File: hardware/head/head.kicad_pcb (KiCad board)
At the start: 2 copper layers, 80 x 55 mm, 59 parts, among them J1 Head bundle, J10 CM4 socket 101-200, J11 Ext amp, J12 Ext 5V, J13 SPI pads, J2 ToF, J3 I2C breakout, J4 Eye LED, J5 Speaker, J6 Fan, J7 Microphone, J8 Camera, J9 CM4 socket 1-100, Q1 AO3400A, U2 LMR51635YDDCR, U3 AMS1117-3.3, U4 MAX98357AETE+T, U5 BMI088

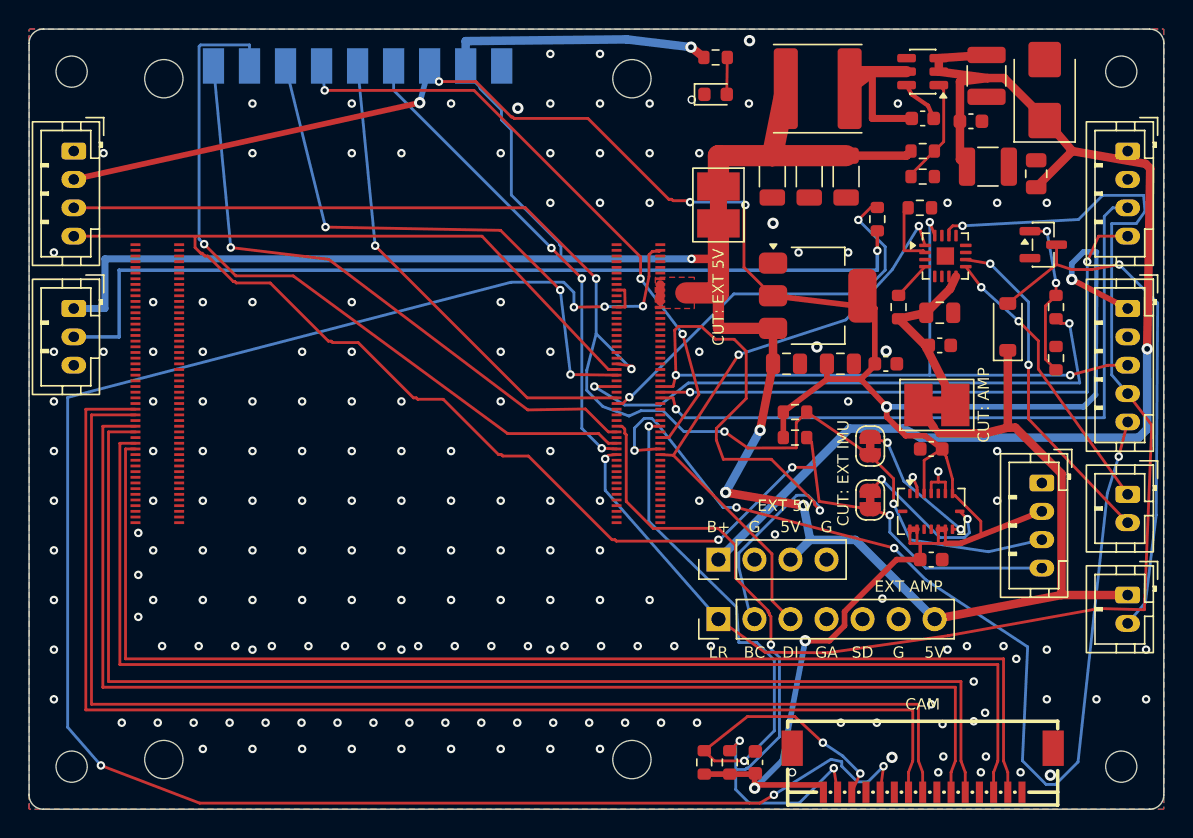
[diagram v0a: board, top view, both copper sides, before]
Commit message: Head carrier PCB rev B: pre-order review changes, USB download pads
- Buck input loop: C4 straight across U2's VIN and GND pins with ground
  vias beside them; boot cap and feedback divider at their pins.
- Input chain J1, TVS, C17 (47 uF 50 V electrolytic, C970679), then the
  ceramics; C3 dropped; fan parts moved down.
- 330R series resistors (R13, R14) in the link UART; J1 pins 3 and 4
  are now LINK_RX and LINK_TX.
- Bottom test pads: RST and BOOT (CM4 pins 92, 93), and USB D+, D-, G
  for the RK3576 download port (pins 105, 103) to flash in place.
  Pins checked against Radxa's CM4 schematic v1.20, sheets 8, 21, 22.
- J13 moved 2.5 mm clear of the module's M2.5 holes; J8 ends marked
  1 GND and 15 3V3.
- Top-layer keep-outs across the cut lines of JP1, JP3, JP4 and JP5
  (no tracks, vias or pour); crossing tracks rerouted.
- Tools: tidy and route_one_net treat locked copper of other nets as
  obstacles; tidy takes a board name, keeps socket ground tracks, never
  straightens through a pad, undangle runs one pass per process;
  route_one_net takes PCB, W, SRC and DST from the environment.
- DRC 0 violations with schematic parity; J9 pad 23 (ground, boxed in)
  unconnected, grounded inside the module. JLC package, PDFs and renders
  regenerated; design note sections 4 and 9.4.
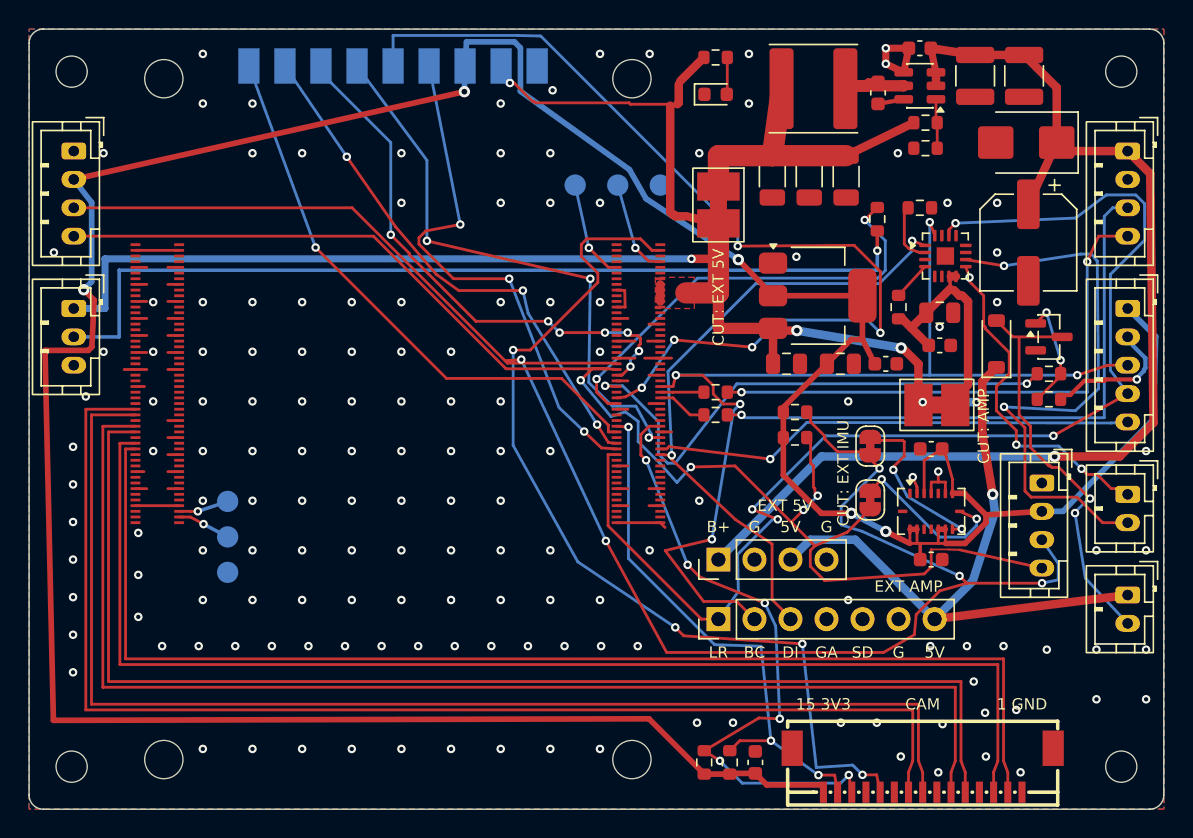
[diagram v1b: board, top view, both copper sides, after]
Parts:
- removed C3: 2.2u 50V, Capacitor_SMD:C_0805_2012Metric
- added C17: 47u 50V, Capacitor_SMD:CP_Elec_6.3x7.7, F.Cu at (170.4, 65.0)
- added R13: 330R, Resistor_SMD:R_0603_1608Metric, F.Cu at (148.4, 77.2)
- added R14: 330R, Resistor_SMD:R_0603_1608Metric, F.Cu at (148.4, 75.6)
- added TP1: CM4_RESET, TestPoint:TestPoint_Pad_D1.5mm, B.Cu at (138.5, 61.0)
- added TP2: CM4_MASKROM, TestPoint:TestPoint_Pad_D1.5mm, B.Cu at (141.5, 61.0)
- added TP3: GND, TestPoint:TestPoint_Pad_D1.5mm, B.Cu at (144.5, 61.0)
- added TP4: USB_DN, TestPoint:TestPoint_Pad_D1.5mm, B.Cu at (114.0, 85.8)
- added TP5: USB_DP, TestPoint:TestPoint_Pad_D1.5mm, B.Cu at (114.0, 83.3)
- added TP6: GND, TestPoint:TestPoint_Pad_D1.5mm, B.Cu at (114.0, 88.3)
- moved C2 6.89 mm to (170.2, 53.3), turned to -90 degrees
- moved Q1 6.51 mm to (171.9, 71.7)
- moved C4 6.28 mm to (162.8, 51.4), turned to 180 degrees
- moved R5 4.73 mm to (171.9, 74.3), turned to 0 degrees
- moved D1 3.92 mm to (170.3, 58.0), turned to 180 degrees
- moved C5 3.63 mm to (159.8, 54.5), turned to 90 degrees
- moved R6 2.94 mm to (171.9, 76.1), turned to 0 degrees
- moved J13 2.50 mm to (135.8, 52.6)
- moved R1 2.01 mm to (163.2, 56.6)
- moved R2 2.01 mm to (163.2, 58.4), turned to 180 degrees
- moved D2 1.44 mm to (168.2, 72.2)
- moved U2 1.02 mm to (162.8, 54.0)
- moved C1 0.80 mm to (166.7, 53.3)
- moved L1 0.30 mm to (155.3, 54.2)
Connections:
- J1 pad 3: /UART7_RX -> /LINK_RX
- J1 pad 4: /UART7_TX -> /LINK_TX
- J10 pad 103: unconnected-(J10-USB2_N-Pad103) -> /USB_DN
- J10 pad 105: unconnected-(J10-USB2_P-Pad105) -> /USB_DP
- J9 pad 92: unconnected-(J9-RUN_PG-Pad92) -> /CM4_RESET
- J9 pad 93: unconnected-(J9-nRPIBOOT-Pad93) -> /CM4_MASKROM
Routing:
- net /CAM_GPIO: track 134.0 -> 65.4 mm, vias 6 -> 4
- net +3V3: track 180.7 -> 241.1 mm, vias 8 -> 5
- net GND: track 4.56 -> 61.7 mm, vias 181 -> 153
- net /UART7_RX: track 48.3 -> 3.57 mm, vias 1 -> 0
- net /LINK_RX: track 0.00 -> 42.8 mm, vias 0 -> 1
- net /SAI2_SDI: track 74.7 -> 34.1 mm, vias 4 -> 1
- net /UART7_TX: track 43.3 -> 3.07 mm, vias 2 -> 0
- net /LINK_TX: track 0.00 -> 38.6 mm, vias 0 -> 2
- net /SPI2_MISO: track 34.2 -> 70.0 mm, vias 1 -> 5
- net /I2C8_SDA: track 92.8 -> 121.2 mm, vias 4 -> 5
- net /I2C8_SCL: track 120.1 -> 98.7 mm, vias 3 -> 4
- net /SPK_N: track 23.9 -> 40.6 mm
- net /SPI_INT: track 53.1 -> 37.6 mm, vias 1 -> 3
- net +5V: track 170.9 -> 158.7 mm, vias 5 -> 7
- net /SAI2_SCLK: track 84.3 -> 73.0 mm, vias 4 -> 5
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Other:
- board text added: "1 GND"
- board text added: "15 3V3"
- board text added: "BOOT"
- board text added: "D+"
- board text added: "D-"
- board text added: "RST"
- board text added: "USB"
- board text added: "rev B 2026"
- board text removed: "rev A 2026"

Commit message: Head carrier PCB: PWM pad for a possible mouth servo
- TP7, a bottom pad beside J9 on CM4 pin 37 (GPIO7, RK3576 GPIO1_C0,
  PWM0_CH0_M1), in case the mouth J288 is swapped for a hobby servo. The
  servo would run from its own buck module fed from J12's B+ and G, not
  the head's 5 V buck. PWM0 is separate from the fan's PWM1.
- Pin 48 (PWM1_CH0_M2) was tried first; on J9's inner row it is boxed in.
- Design note: J13 already gives spare GPIOs with 3V3 and GND (pads 8, 9
  and the SPI2 lines); a separate breakout under the module was tried and
  dropped (only a 130 mm, 11-via route).
- DRC 0 violations with schematic parity (J9 pad 23 as before); JLC
  package, PDFs and bottom render regenerated.
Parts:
- added TP7: SERVO_PWM, TestPoint:TestPoint_Pad_D1.5mm, B.Cu at (146.6, 77.0)
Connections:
- J9 pad 37: unconnected-(J9-GPIO7-Pad37) -> /SERVO_PWM
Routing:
- net /SERVO_PWM: track 0.00 -> 1.22 mm, vias 0 -> 1
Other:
- board text added: "PWM"
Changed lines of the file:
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@@
 			(size 0.2 0.7)
 			(layers "F.Cu" "F.Mask" "F.Paste")
-			(net "unconnected-(J9-GPIO7-Pad37)")
+			(net "/SERVO_PWM")
 		)
 		(pad "38" smd rect
@@
 		(locked yes)
 		(layer "B.Cu")
+		(at 146.55 77 180)
+		(descr "SMD pad as test Point, diameter 1.5mm")
+		(tags "test point SMD pad")
+		(property "Reference" "TP7"
+			(at 0 1.648 0)
+			(layer "B.Fab")
+			(effects
+				(font
+					(size 1 1)
+					(thickness 0.15)
+				)
+				(justify mirror)
+			)
+		)
+		(property "Value" "SERVO_PWM"
+			(at 0 -1.75 0)
+			(layer "B.Fab")
+			(hide yes)
+			(effects
+				(font
+					(size 1 1)
+					(thickness 0.15)
+				)
+				(justify mirror)
+			)
+		)
+		(property "Datasheet" ""
+			(at 0 0 0)
+			(unlocked yes)
+			(layer "B.Fab")
+			(hide yes)
+			(effects
+				(font
+					(size 1.27 1.27)
+					(thickness 0.15)
+				)
+				(justify mirror)
+			)
+		)
+		(property "Description" ""
+			(at 0 0 0)
+			(unlocked yes)
+			(layer "B.Fab")
+			(hide yes)
+			(effects
+				(font
+					(size 1.27 1.27)
+					(thickness 0.15)
+				)
+				(justify mirror)
+			)
+		)
+		(sheetname "Root")
+		(sheetfile "head.kicad_sch")
+		(attr exclude_from_pos_files exclude_from_bom)
+		(duplicate_pad_numbers_are_jumpers no)
+		(fp_circle
+			(center 0 0)
+			(end 0 -0.95)
+			(stroke
+				(width 0.12)
+				(type solid)
+			)
+			(fill no)
+			(layer "B.SilkS")
+		)
+		(fp_circle
+			(center 0 0)
+			(end 1.25 0)
+			(stroke
+				(width 0.05)
+				(type solid)
+			)
+			(fill no)
+			(layer "B.CrtYd")
+		)
+		(fp_text user "${REFERENCE}"
+			(at 0 1.65 0)
+			(layer "B.Fab")
+			(effects
+				(font
+					(size 1 1)
+					(thickness 0.15)
+				)
+				(justify mirror)
+			)
+		)
+		(pad "1" smd circle
+			(at 0 0 180)
+			(size 1.5 1.5)
+			(layers "B.Cu" "B.Mask")
+			(net "/SERVO_PWM")
+		)
+		(embedded_fonts no)
+	)
+	(footprint "TestPoint:TestPoint_Pad_D1.5mm"
+		(locked yes)
+		(layer "B.Cu")
 		(at 114 85.8 180)
 		(descr "SMD pad as test Point, diameter 1.5mm")
@@
 		)
 	)
+	(gr_text "PWM"
+		(at 148.95 77 0)
+		(layer "B.SilkS")
+		(effects
+			(font
+				(size 0.8 0.8)
+				(thickness 0.15)
+			)
+			(justify mirror)
+		)
+	)
 	(gr_text "1"
 		(at 169.3 80.1 0)
@@
 	)
 	(segment
+		(start 145.6 77.6)
+		(end 145.9 77.3)
+		(width 0.2)
+		(locked yes)
+		(layer "F.Cu")
+		(net "/SERVO_PWM")
+	)
+	(segment
+		(start 144.8 77.6)
+		(end 145.6 77.6)
+		(width 0.2)
+		(locked yes)
+		(layer "F.Cu")
+		(net "/SERVO_PWM")
+	)
+	(via
+		(at 145.9 77.3)
+		(size 0.6)
+		(drill 0.3)
+		(layers "F.Cu" "B.Cu")
+		(locked yes)
+		(net "/SERVO_PWM")
+	)
+	(segment

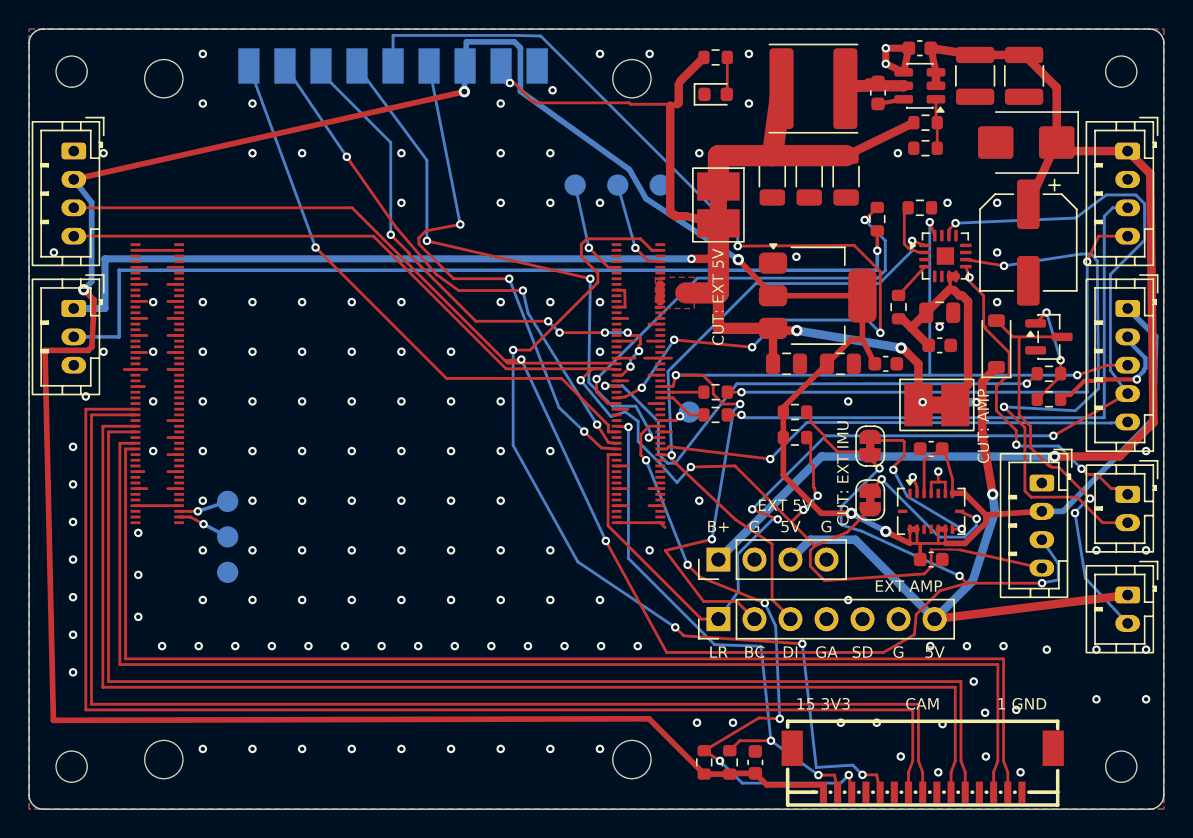
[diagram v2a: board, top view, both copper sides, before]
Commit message: Head PCB: rev B second review, head_ext variant with the BMI088 module
Rev B (hardware/head), second pre-order review (docs/head-pcb.md 9.5):
- R13 1k on the link RX line; J13's 5 V re-routed clear of the module
  hole; ground vias and solid ground pads at C1, C2, D1 and C17; 3.3 V
  copper on the AMS1117 tab
- CM4 orientation marks (CM4 U.FL END, pin 1 and 101 dots); J11 and J12
  names on the back
- polarity picture for JLC's placement preview

head_ext (hardware/head_ext, 9.6): rev B with the generic BMI088 module
hand-fitted in place of the chip, so the board needs only Economic PCBA
- U5 chip, C15, C16, JP4, JP5, R8, R9 and the J3 PH header removed
- module on the front, rows 11.3 mm apart; I2C8 pins (J3, 2.0 mm) and
  J12 on the right edge; J11 as bottom-side solder pads
- pin names on both sides; re-routed locally with Freerouting and the
  maze router; DRC clean with schematic parity
- reviewed against rev B: netlist, rev B's fixes, re-routed nets, silk,
  JLC stock

Placement: export_jlc.py now corrects the CPL rotation (and origin)
where JLC's EasyEDA footprint is turned from ours: the DF40C sockets,
SOT-23, SOT-23-6, SOT-223, TQFN-16 and LGA-16 on the head boards, and
the bridge's hand fixes of a4dfda9, which it now reproduces.

Tools: gen_head_sch.py --variant head_ext, sync_head_pcb.py --board and
--prune, make_head_ext_pcb.py, rip_under_pads.py, nudge_fp.py; tidy,
finish and polarity scripts take the board name; undangle keeps a via
inside a same-net pad.
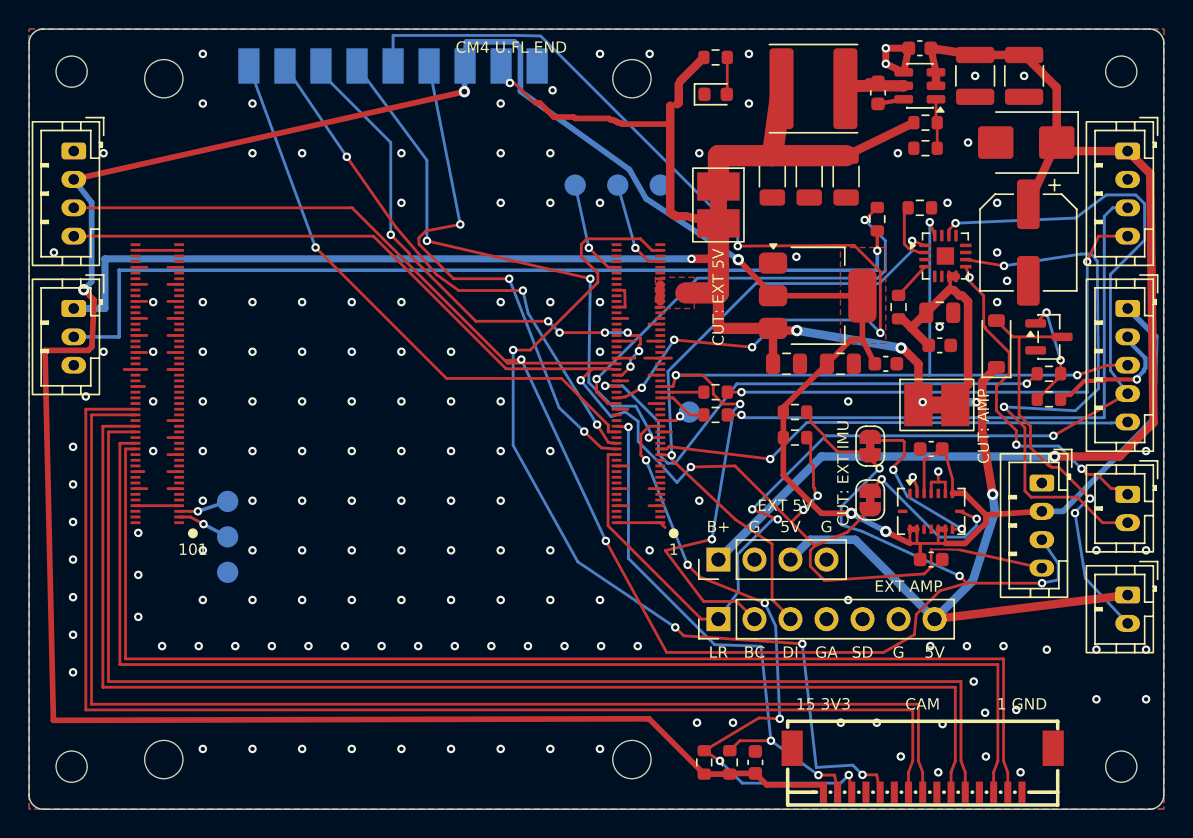
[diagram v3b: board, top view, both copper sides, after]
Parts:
- R13: value 330R -> 1k
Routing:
- net GND: vias 153 -> 157
- added copper zone on F.Cu, net +3V3
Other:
- board text added: "101"
- board text added: "CM4 U.FL END"
